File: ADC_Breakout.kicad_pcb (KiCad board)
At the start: 2 copper layers, 55 x 55 mm, 69 parts, among them J0 Conn_01x06, J10 Conn_01x02, J11 Conn_01x02, J12 Conn_01x02, J13 Conn_01x02, J2 Digital Power, J3 Clock Chooser, J4 Analog Power, J6 Conn_01x02, J7 Conn_01x02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

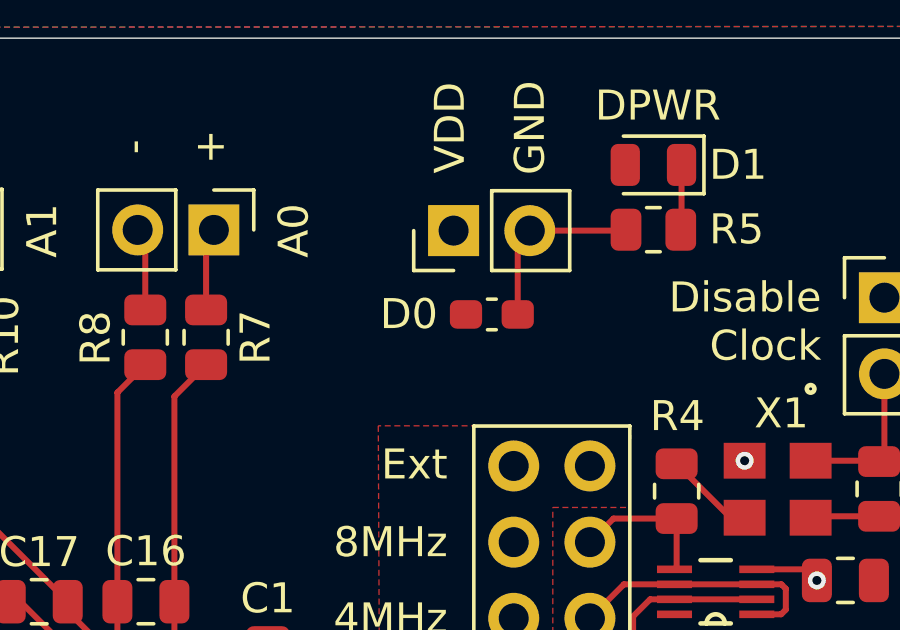
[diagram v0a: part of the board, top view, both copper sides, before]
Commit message: Updated footprint.
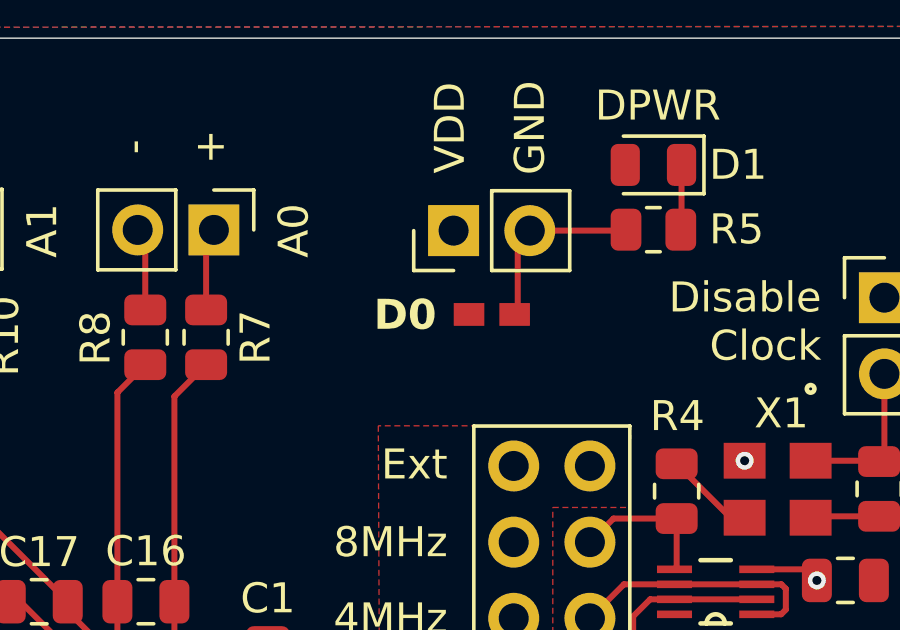
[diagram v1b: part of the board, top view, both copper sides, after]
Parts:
- D0: footprint Capacitor_SMD:C_0603_1608Metric_Pad1.08x0.95mm_HandSolder -> TVS:VAR_CG0603MLU-3.3E
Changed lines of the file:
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@@
 		)
 	)
-	(footprint "Capacitor_SMD:C_0603_1608Metric_Pad1.08x0.95mm_HandSolder"
+	(footprint "TVS:VAR_CG0603MLU-3.3E"
 		(layer "F.Cu")
 		(at 142.24 84.709)
-		(descr "Capacitor SMD 0603 (1608 Metric), square (rectangular) end terminal, IPC_7351 nominal with elongated pad for handsoldering. (Body size source: IPC-SM-782 page 76, https://www.pcb-3d.com/wordpress/wp-content/uploads/ipc-sm-782a_amendment_1_and_2.pdf), generated with kicad-footprint-generator")
-		(tags "capacitor handsolder")
 		(property "Reference" "D0"
-			(at -2.765 -0.009 0)
+			(at -2.89 0.016 0)
 			(layer "F.SilkS")
 			(effects
@@
 					(size 1 1)
 					(thickness 0.153)
+					(bold yes)
 				)
 			)
 		)
 		(property "Value" "D_TVS_Small"
-			(at 0 1.43 0)
+			(at 7.49 1.56 0)
 			(layer "F.Fab")
 			(effects
 				(font
-					(size 1 1)
+					(size 0.787402 0.787402)
 					(thickness 0.15)
 				)
 			)
 		)
-		(property "Footprint" "Capacitor_SMD:C_0603_1608Metric_Pad1.08x0.95mm_HandSolder"
+		(property "Footprint" "TVS:VAR_CG0603MLU-3.3E"
 			(at 0 0 0)
-			(unlocked yes)
 			(layer "F.Fab")
 			(hide yes)
@@
 		(property "Datasheet" ""
 			(at 0 0 0)
-			(unlocked yes)
 			(layer "F.Fab")
 			(hide yes)
@@
 		(property "Description" "Bidirectional transient-voltage-suppression diode, small symbol"
 			(at 0 0 0)
-			(unlocked yes)
 			(layer "F.Fab")
 			(hide yes)
@@
 		(attr smd)
 		(fp_line
-			(start -0.146267 -0.51)
-			(end 0.146267 -0.51)
-			(stroke
-				(width 0.12)
-				(type solid)
-			)
-			(layer "F.SilkS")
-		)
-		(fp_line
-			(start -0.146267 0.51)
-			(end 0.146267 0.51)
-			(stroke
-				(width 0.12)
-				(type solid)
-			)
-			(layer "F.SilkS")
-		)
-		(fp_line
-			(start -1.65 -0.73)
-			(end 1.65 -0.73)
+			(start -1.52 -0.65)
+			(end -1.52 0.65)
 			(stroke
 				(width 0.05)
@@
 		)
 		(fp_line
-			(start -1.65 0.73)
-			(end -1.65 -0.73)
+			(start -1.52 0.65)
+			(end 1.52 0.65)
 			(stroke
 				(width 0.05)
@@
 		)
 		(fp_line
-			(start 1.65 -0.73)
-			(end 1.65 0.73)
+			(start 1.52 -0.65)
+			(end -1.52 -0.65)
 			(stroke
 				(width 0.05)
@@
 		)
 		(fp_line
-			(start 1.65 0.73)
-			(end -1.65 0.73)
+			(start 1.52 0.65)
+			(end 1.52 -0.65)
 			(stroke
 				(width 0.05)
@@
 			(end 0.8 -0.4)
 			(stroke
-				(width 0.1)
+				(width 0.127)
 				(type solid)
 			)
@@
 			(end -0.8 -0.4)
 			(stroke
-				(width 0.1)
+				(width 0.127)
 				(type solid)
 			)
@@
 			(end 0.8 0.4)
 			(stroke
-				(width 0.1)
+				(width 0.127)
 				(type solid)
 			)
@@
 			(end -0.8 0.4)
 			(stroke
-				(width 0.1)
+				(width 0.127)
 				(type solid)
 			)
 			(layer "F.Fab")
 		)
-		(fp_text user "${REFERENCE}"
-			(at 0 0 0)
-			(layer "F.Fab")
-			(effects
-				(font
-					(size 0.4 0.4)
-					(thickness 0.06)
-				)
-			)
-		)
-		(pad "1" smd roundrect
-			(at -0.8625 0)
-			(size 1.075 0.95)
+		(pad "1" smd rect
+			(at -0.76 0)
+			(size 1.02 0.76)
 			(layers "F.Cu" "F.Paste" "F.Mask")
-			(roundrect_rratio 0.25)
 			(net 3 "VDD")
 			(pinfunction "A1")
 			(pintype "passive")
+			(solder_mask_margin 0.102)
 		)
-		(pad "2" smd roundrect
-			(at 0.8625 0)
-			(size 1.075 0.95)
+		(pad "2" smd rect
+			(at 0.76 0)
+			(size 1.02 0.76)
 			(layers "F.Cu" "F.Paste" "F.Mask")
-			(roundrect_rratio 0.25)
 			(net 1 "GND")
 			(pinfunction "A2")
 			(pintype "passive")
-		)
-		(model "${KICAD8_3DMODEL_DIR}/Capacitor_SMD.3dshapes/C_0603_1608Metric.wrl"
-			(offset
-				(xyz 0 0 0)
-			)
-			(scale
-				(xyz 1 1 1)
-			)
-			(rotate
-				(xyz 0 0 0)
-			)
+			(solder_mask_margin 0.102)
 		)
 	)
